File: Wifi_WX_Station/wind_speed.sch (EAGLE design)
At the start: 10 parts, among them T1 MMBT3904

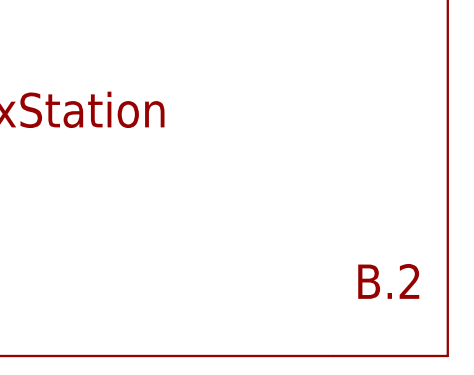
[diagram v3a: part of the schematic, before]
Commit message: Added multiple new boards - H-pwrdist- Insp_Wind_enc, 5040 etc..
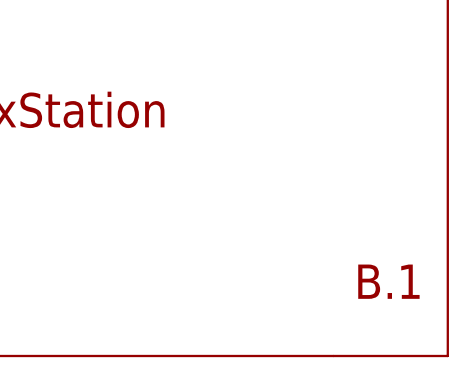
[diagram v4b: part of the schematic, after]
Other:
- note added: "B.1"
- note removed: "B.2"
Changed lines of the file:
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@@
 <plain>
 <text x="195.58" y="2.54" size="3.81" layer="94" ratio="20">WunderWxStation</text>
-<text x="258.826" y="-16.51" size="3.81" layer="94" ratio="20">B.2</text>
+<text x="258.826" y="-16.51" size="3.81" layer="94" ratio="20">B.1</text>
 </plain>
 <instances>
